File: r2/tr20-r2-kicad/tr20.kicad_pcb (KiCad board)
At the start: 4 copper layers, 110.2 x 145.8 mm, 233 parts, among them J1 532610271, J10 PJ-320D, J2 USB-C-12, J3 UJ2-AH-1-SMT, J4 TF-15x15, J5 AFC07-S24ECA-00, J6 DNP, J7 2x03-socket-2.54-through-board, J8 DNP, J9 532610271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

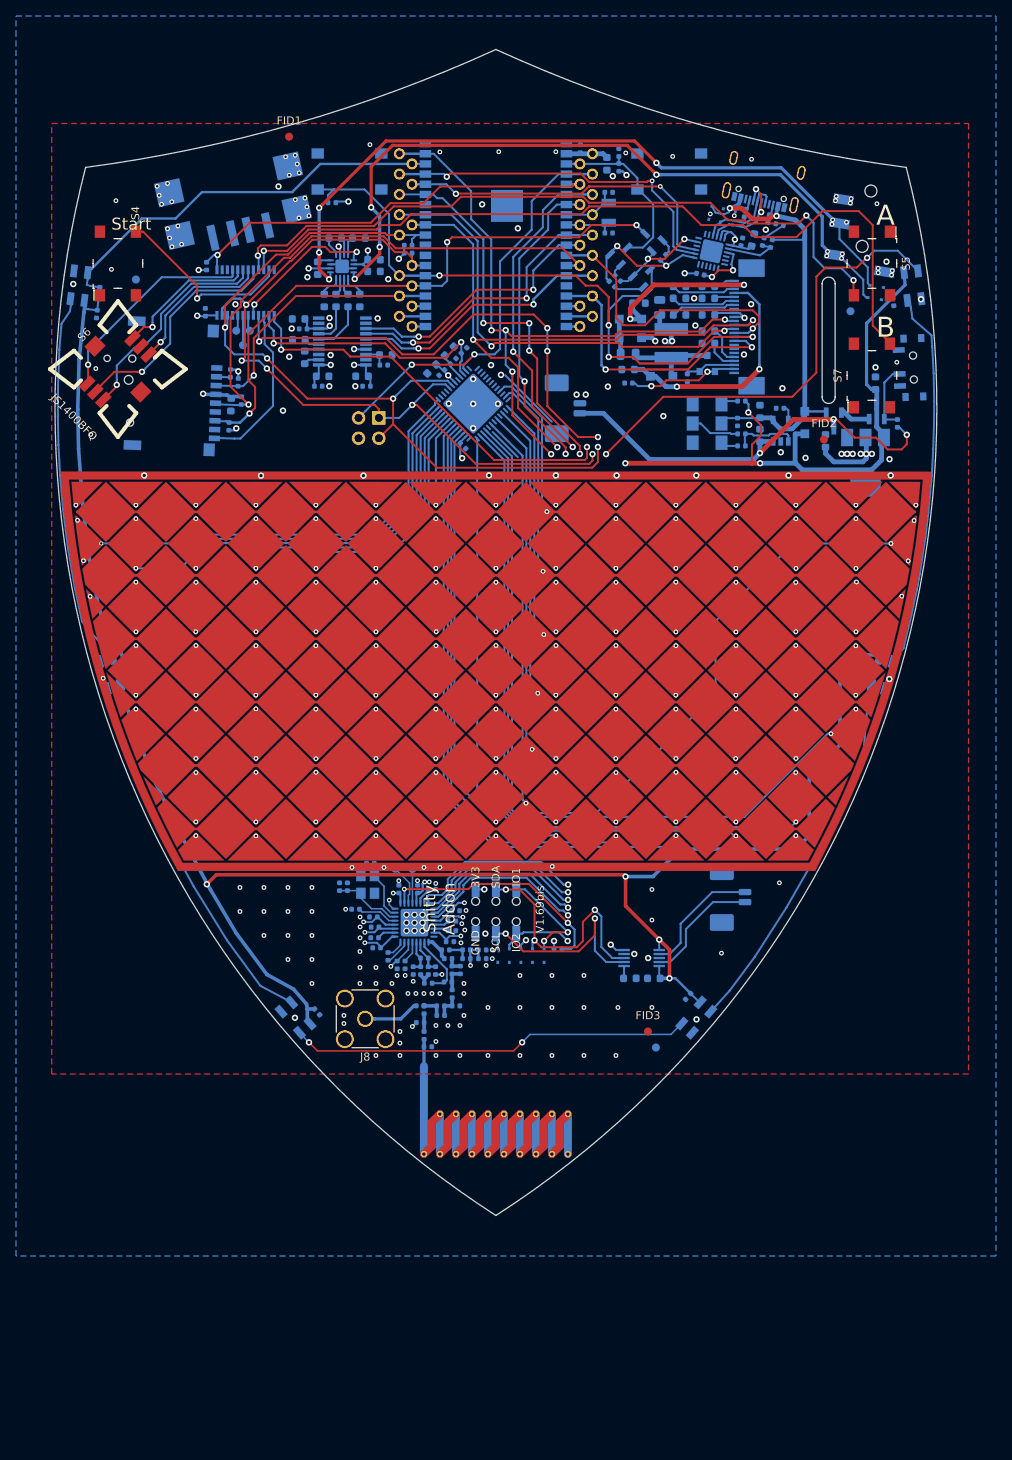
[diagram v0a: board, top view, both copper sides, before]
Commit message: Update footprints, DRC items
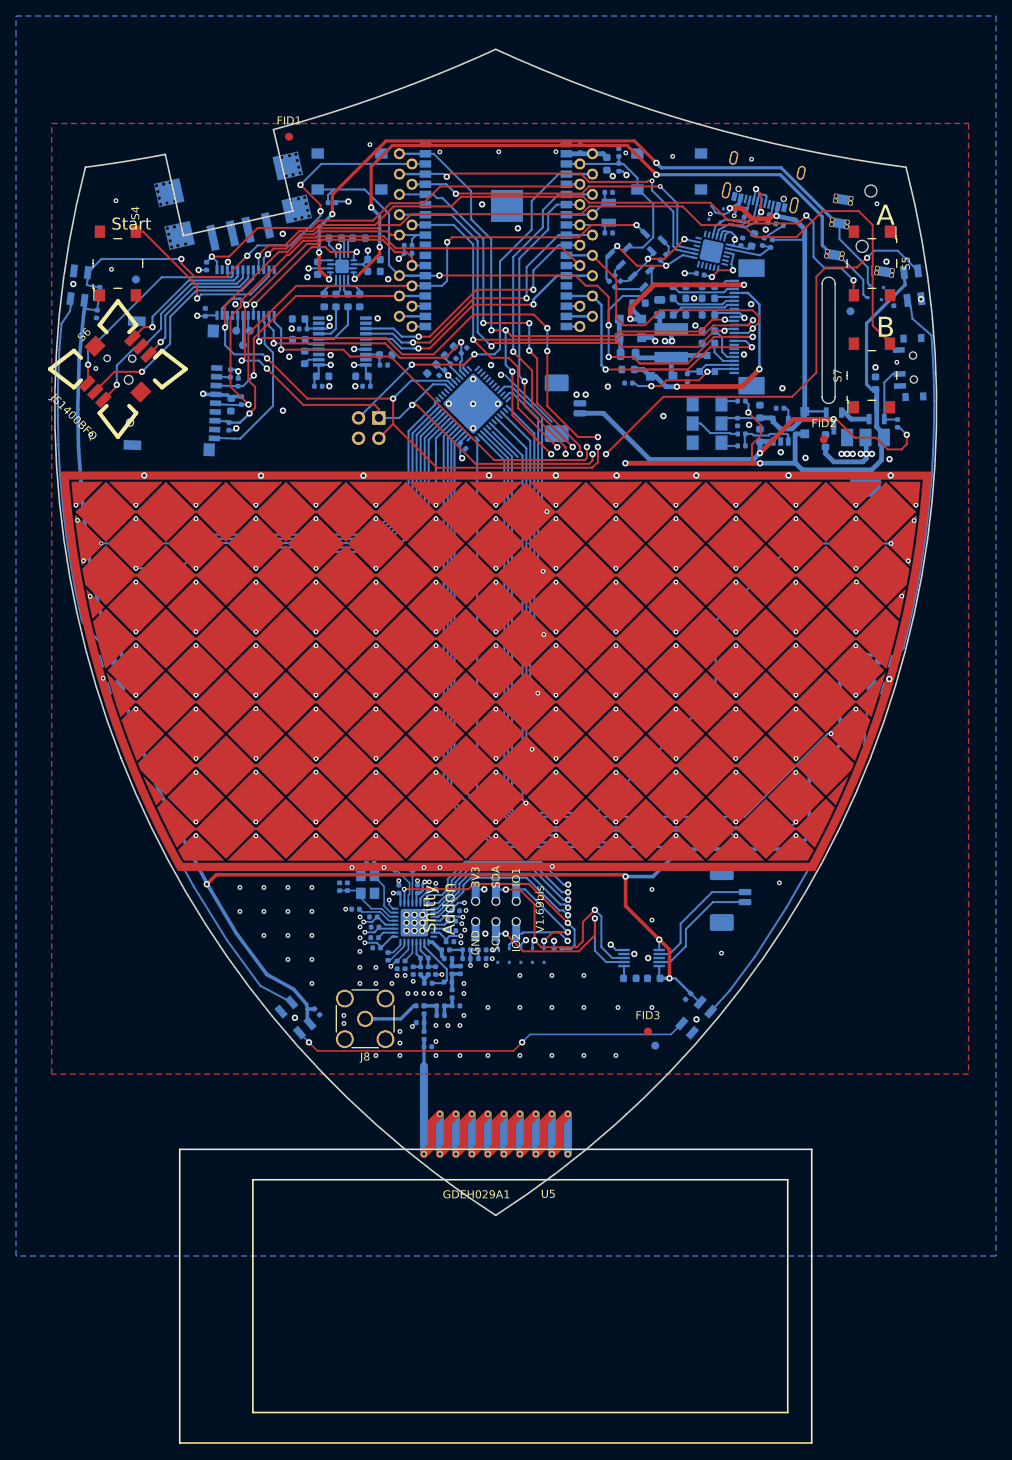
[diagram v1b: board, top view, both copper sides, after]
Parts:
- added U5: GDEH029A1, jeffmakes-footprints:GDEH029A1, F.Cu at (-0.02, 10.1)
- J10: footprint Connector_Audio:Jack_3.5mm_PJ320D_Horizontal -> Connector_Audio:Jack_3.5mm_PJ320D_Horizontal_strengthening-vias
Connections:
- J10 pad R2: (no net) -> Net-(J10-PadR2)
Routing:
- net /LED_DIN: track 51.3 -> 60.0 mm, vias 0 -> 4
- net /io_expander/BTN_A: track 89.4 -> 88.9 mm
- net /audio/OUTR: vias 7 -> 4
- net GND: vias 191 -> 168
- net /audio/OUTL: vias 8 -> 4
- net (no net): vias 4 -> 0
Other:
- outline, holes or cut-outs redrawn
